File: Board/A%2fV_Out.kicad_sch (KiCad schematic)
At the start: 21 parts, among them IC2 74HCT245DW, X2 D-SUB15-HDR15RA

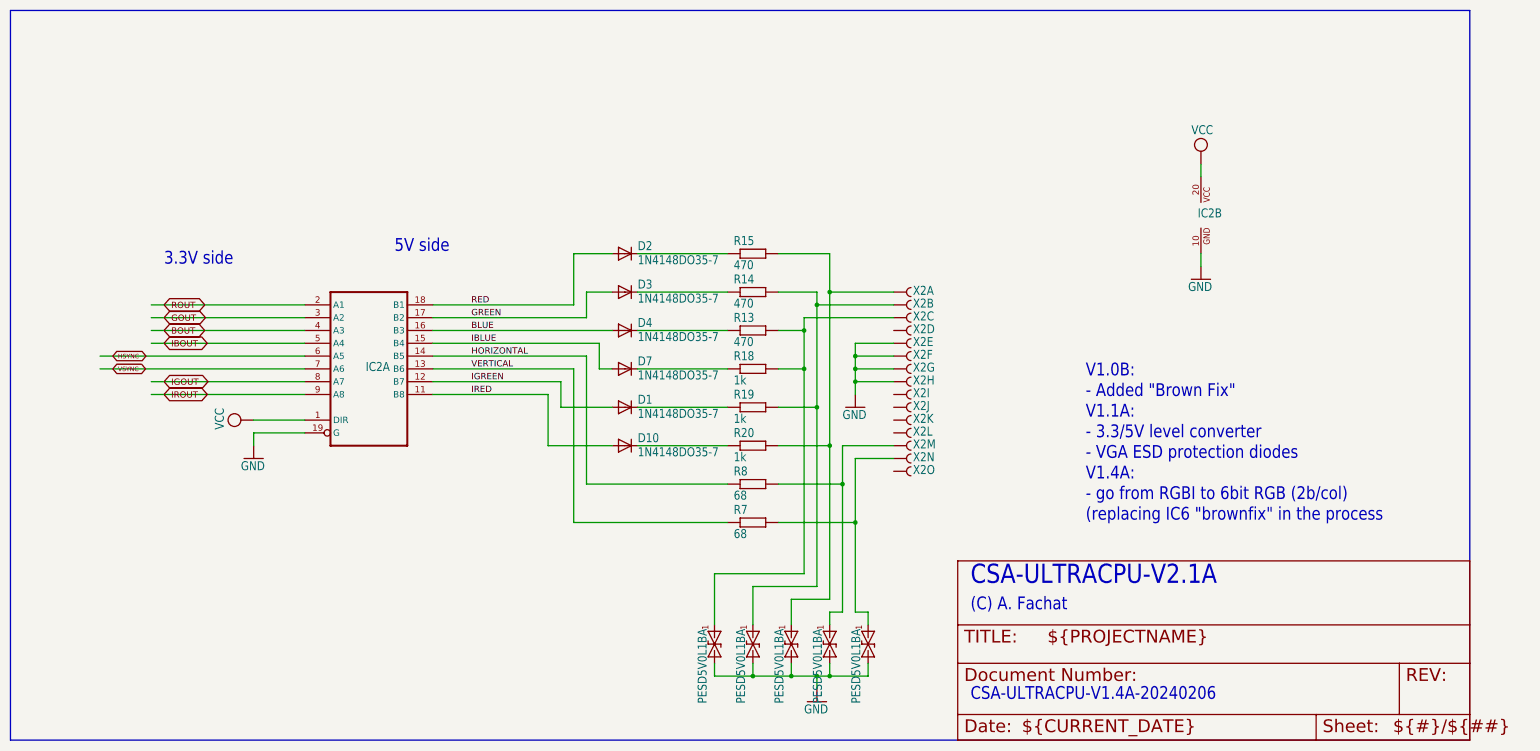
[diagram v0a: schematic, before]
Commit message: start r2.2a, moving from VGA to HDMI
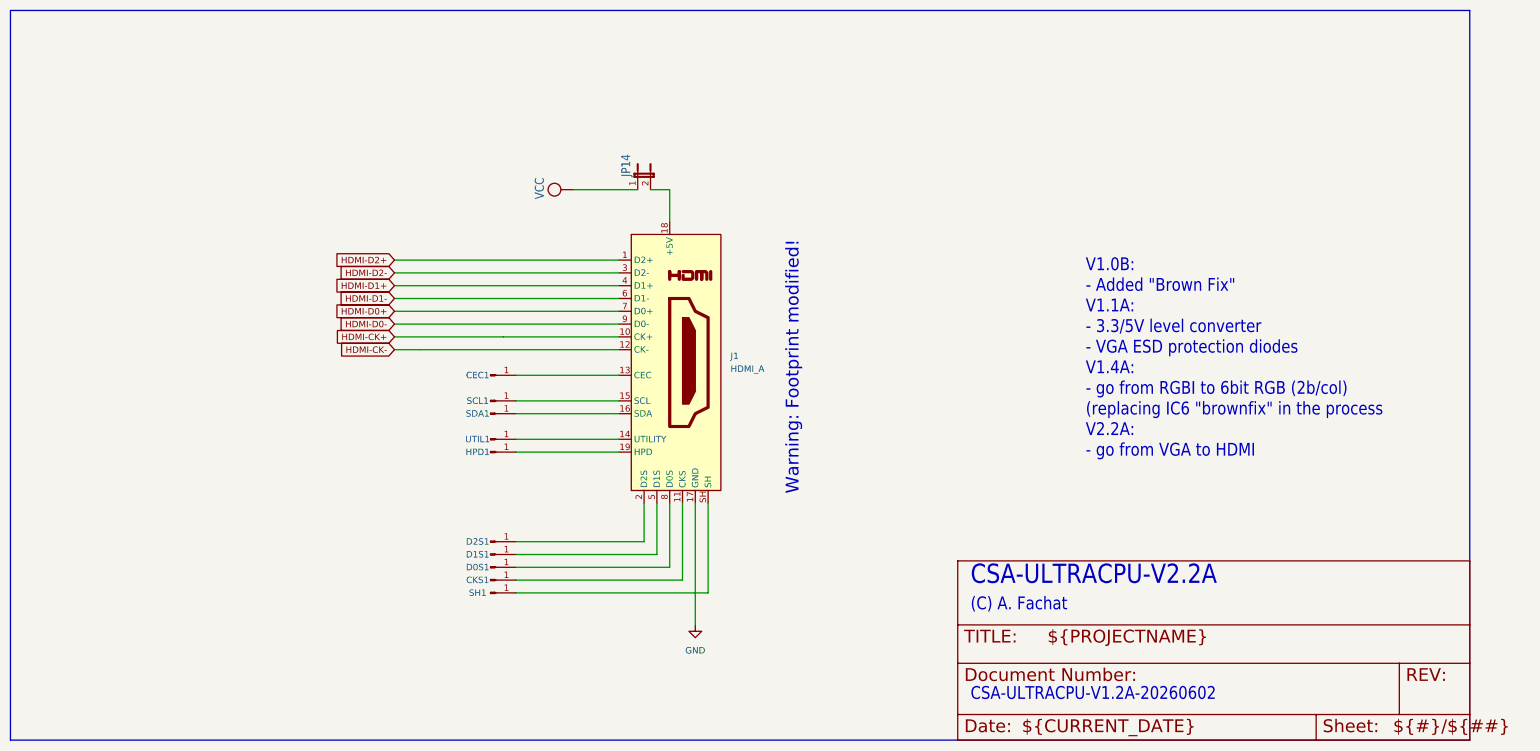
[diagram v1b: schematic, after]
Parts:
- removed D1, D10, D2, D3, D4, D7: 1N4148DO35-7, csa_ultracpu:DO35-7, symbol csa_ultracpu-eagle-import:1N4148DO35-7
- removed IC2: 74HCT245DW, csa_ultracpu:SO20W, symbol csa_ultracpu-eagle-import:74245DW
- removed R13, R14, R15: 470, csa_ultracpu:0204V, symbol csa_ultracpu-eagle-import:R-EU_0204/2V
- removed R18, R19, R20: 1k, csa_ultracpu:0204V, symbol csa_ultracpu-eagle-import:R-EU_0204/2V
- removed R7, R8: 68, csa_ultracpu:0204V, symbol csa_ultracpu-eagle-import:R-EU_0204/2V
- removed U$10, U$11, U$5, U$6, U$8: PESD5V0L1BA, csa_ultracpu:SOD323, symbol csa_ultracpu-eagle-import:ESDBIDIR
- removed X2: D-SUB15-HDR15RA, csa_ultracpu:HDR15RA, symbol csa_ultracpu-eagle-import:D-SUB15-HDR15RA
- added CEC1, CKS1, D0S1, D1S1, D2S1, HPD1, SCL1, SDA1, SH1, UTIL1: Conn_01x01_Pin, Connector_PinHeader_1.00mm:PinHeader_1x01_P1.00mm_Vertical, symbol Connector:Conn_01x01_Pin
- added J1: HDMI_A, Connector_Video:HDMI_A_Molex_208658-1001_Horizontal, symbol Connector:HDMI_A
- added JP14: JP1E, csa_ultracpu:JP1, symbol csa_ultracpu-eagle-import:JP1E
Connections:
- net GND: now also J1.17 (GND)
- net VCC: now also JP14.1
- new net: J1.SH, SH1.1 (Pin_1)
- new net: J1.14 (UTILITY), UTIL1.1 (Pin_1)
- new net: J1.15 (SCL), SCL1.1 (Pin_1)
- new net: J1.18 (+5V), JP14.2
- new net: HPD1.1 (Pin_1), J1.19 (HPD)
- new net: D2S1.1 (Pin_1), J1.2 (D2S)
- new net: CKS1.1 (Pin_1), J1.11 (CKS)
- new net: D1S1.1 (Pin_1), J1.5 (D1S)
- new net: D0S1.1 (Pin_1), J1.8 (D0S)
- new net: CEC1.1 (Pin_1), J1.13 (CEC)
- new net: J1.16 (SDA), SDA1.1 (Pin_1)
- new net HDMI-CK+: J1.10 (CK+)
- new net HDMI-CK-: J1.12 (CK-)
- new net HDMI-D0+: J1.7 (D0+)
- new net HDMI-D0-: J1.9 (D0-)
- new net HDMI-D1+: J1.4 (D1+)
- new net HDMI-D1-: J1.6 (D1-)
- new net HDMI-D2+: J1.1 (D2+)
- new net HDMI-D2-: J1.3 (D2-)
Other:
- note added: "CSA-ULTRACPU-V1.2A-20260602"
- note added: "CSA-ULTRACPU-V2.2A"
- note added: "V1.0B: - Added "Brown Fix" V1.1A: - 3.3/5V level converter - VGA ESD protection diodes V1.4A: - go from RGBI to 6bit RGB (2b/col) (replacing IC6 "brownfix" in the process V2.2A: - go from VGA to HDMI"
- note added: "Warning: Footprint modified!"
- note removed: "3.3V side"
- note removed: "5V side"
- note removed: "CSA-ULTRACPU-V1.4A-20240206"
- note removed: "CSA-ULTRACPU-V2.1A"
- note removed: "V1.0B: - Added "Brown Fix" V1.1A: - 3.3/5V level converter - VGA ESD protection diodes V1.4A: - go from RGBI to 6bit RGB (2b/col) (replacing IC6 "brownfix" in the process"
